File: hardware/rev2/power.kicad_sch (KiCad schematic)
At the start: 0 parts

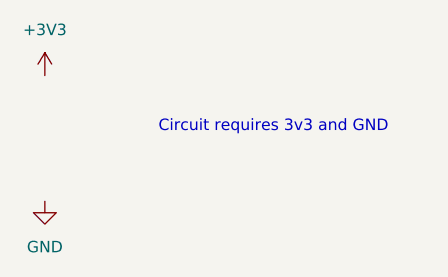
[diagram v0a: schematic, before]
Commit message: fixed some ERC errors and warnings, added USB, assigned a bunch of footprints
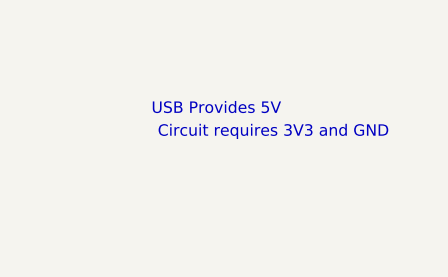
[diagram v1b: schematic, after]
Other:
- note added: "Circuit requires 3V3 and GND"
- note added: "USB Provides 5V"
- note removed: "Circuit requires 3v3 and GND"
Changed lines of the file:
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@@
 	(generator_version "10.0")
 	(paper "A4")
-	(text "Circuit requires 3v3 and GND"
+	(text "USB Provides 5V"
 		(exclude_from_sim no)
-		(at 125.73 80.645 0)
+		(at 119.38 78.74 0)
 		(effects
 			(font
@@
 		)
 	)
-	(symbol
-		(lib_id "power:+3V3")
-		(at 100.33 74.93 0)
-		(unit 1)
-		(body_style 1)
+	(text "Circuit requires 3V3 and GND"
 		(exclude_from_sim no)
-		(in_bom yes)
-		(on_board yes)
-		(in_pos_files yes)
-		(dnp no)
-		(fields_autoplaced yes)
-		(property "Reference" "#PWR059"
-			(at 100.33 78.74 0)
-			(hide yes)
-			(show_name no)
-			(do_not_autoplace no)
-			(effects
-				(font
-					(size 1.27 1.27)
-				)
+		(at 125.73 81.28 0)
+		(effects
+			(font
+				(size 1.27 1.27)
 			)
 		)
-		(property "Value" "+3V3"
-			(at 100.33 69.85 0)
-			(show_name no)
-			(do_not_autoplace no)
-			(effects
-				(font
-					(size 1.27 1.27)
-				)
-			)
-		)
-		(property "Footprint" ""
-			(at 100.33 74.93 0)
-			(hide yes)
-			(show_name no)
-			(do_not_autoplace no)
-			(effects
-				(font
-					(size 1.27 1.27)
-				)
-			)
-		)
-		(property "Datasheet" ""
-			(at 100.33 74.93 0)
-			(hide yes)
-			(show_name no)
-			(do_not_autoplace no)
-			(effects
-				(font
-					(size 1.27 1.27)
-				)
-			)
-		)
-		(property "Description" "Power symbol creates a global label with name \"+3V3\""
-			(at 100.33 74.93 0)
-			(hide yes)
-			(show_name no)
-			(do_not_autoplace no)
-			(effects
-				(font
-					(size 1.27 1.27)
-				)
-			)
-		)
-		(pin "1"
-		)
-		(instances
-			(project "rev2"
-				(path "/9067f306-e23c-4d77-8182-4fa2c4b88902/46484475-7656-401a-9d45-159f5e421427"
-					(reference "#PWR059")
-					(unit 1)
-				)
-			)
-		)
-	)
-	(symbol
-		(lib_id "power:GND")
-		(at 100.33 88.9 0)
-		(unit 1)
-		(body_style 1)
-		(exclude_from_sim no)
-		(in_bom yes)
-		(on_board yes)
-		(in_pos_files yes)
-		(dnp no)
-		(fields_autoplaced yes)
-		(property "Reference" "#PWR060"
-			(at 100.33 95.25 0)
-			(hide yes)
-			(show_name no)
-			(do_not_autoplace no)
-			(effects
-				(font
-					(size 1.27 1.27)
-				)
-			)
-		)
-		(property "Value" "GND"
-			(at 100.33 93.98 0)
-			(show_name no)
-			(do_not_autoplace no)
-			(effects
-				(font
-					(size 1.27 1.27)
-				)
-			)
-		)
-		(property "Footprint" ""
-			(at 100.33 88.9 0)
-			(hide yes)
-			(show_name no)
-			(do_not_autoplace no)
-			(effects
-				(font
-					(size 1.27 1.27)
-				)
-			)
-		)
-		(property "Datasheet" ""
-			(at 100.33 88.9 0)
-			(hide yes)
-			(show_name no)
-			(do_not_autoplace no)
-			(effects
-				(font
-					(size 1.27 1.27)
-				)
-			)
-		)
-		(property "Description" "Power symbol creates a global label with name \"GND\" , ground"
-			(at 100.33 88.9 0)
-			(hide yes)
-			(show_name no)
-			(do_not_autoplace no)
-			(effects
-				(font
-					(size 1.27 1.27)
-				)
-			)
-		)
-		(pin "1"
-		)
-		(instances
-			(project "rev2"
-				(path "/9067f306-e23c-4d77-8182-4fa2c4b88902/46484475-7656-401a-9d45-159f5e421427"
-					(reference "#PWR060")
-					(unit 1)
-				)
-			)
-		)

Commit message: ESP32 approaching final schematic. tidied up a lot and changed GPIO pins.
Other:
- company: (none) -> MMCX11
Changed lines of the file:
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@@
 	(generator_version "10.0")
 	(paper "A4")
+	(title_block
+		(company "MMCX11")
+	)
 	(text "USB Provides 5V"
 		(exclude_from_sim no)

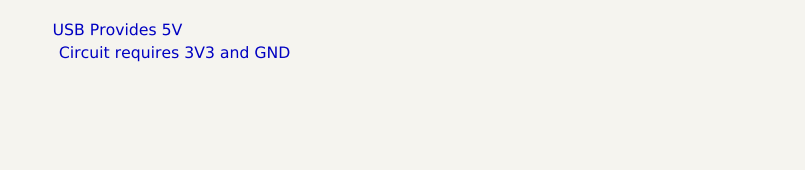
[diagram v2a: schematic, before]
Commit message: set all applicable components for sx1262
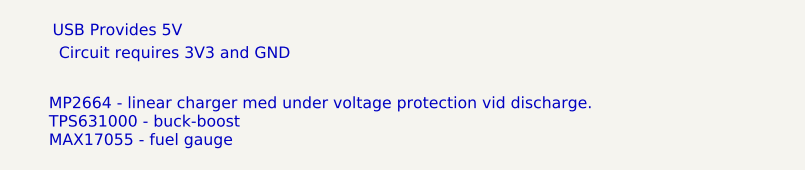
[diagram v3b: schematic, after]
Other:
- note added: "MP2664 - linear charger med under voltage protection vid discharge. TPS631000 - buck-boost MAX17055 - fuel gauge"
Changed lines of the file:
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@@
 		(company "MMCX11")
+	)
+	(text "MP2664 - linear charger med under voltage protection vid discharge.\nTPS631000 - buck-boost\nMAX17055 - fuel gauge"
+		(exclude_from_sim no)
+		(at 111.76 88.9 0)
+		(effects
+			(font
+				(size 1.27 1.27)
+			)
+			(justify left)
+		)
 	)
 	(text "USB Provides 5V"

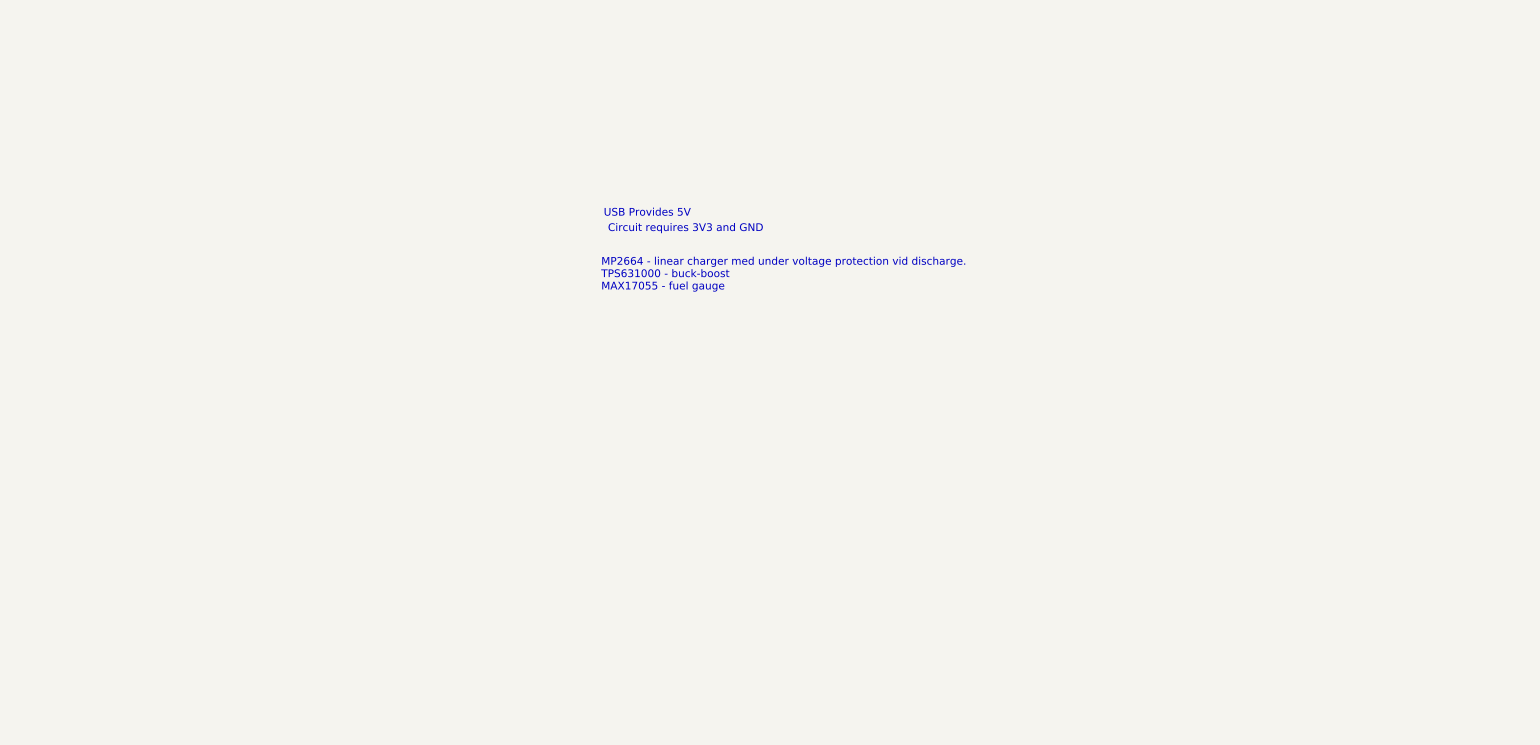
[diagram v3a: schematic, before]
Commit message: Started work on power.kicad_sch
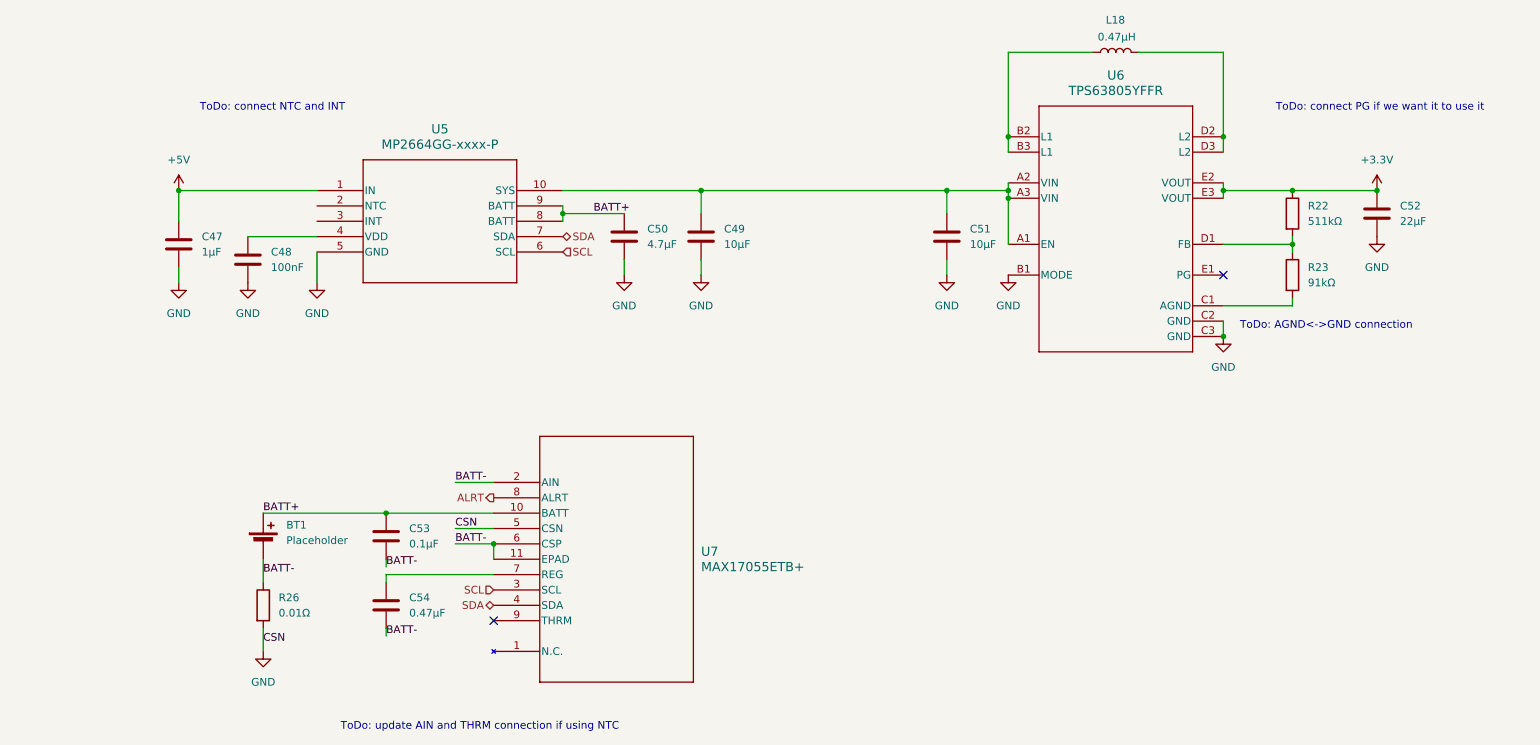
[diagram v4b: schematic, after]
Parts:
- added BT1: Placeholder, symbol Device:Battery_Cell
- added C47: 1µF, symbol Device:C
- added C48: 100nF, symbol Device:C
- added C49, C51: 10µF, symbol Device:C
- added C50: 4.7µF, symbol Device:C
- added C52: 22µF, symbol Device:C
- added C53: 0.1µF, symbol Device:C
- added C54: 0.47µF, symbol Device:C
- added L18: 0.47µH, symbol Device:L
- added R22: 511kΩ, symbol Device:R
- added R23: 91kΩ, symbol Device:R
- added R26: 0.01Ω, symbol Device:R
- added U5: MP2664GG-xxxx-P, QFN-2x2_MP2664_MNP, symbol _symbols:MP2664GG-xxxx-P
- added U6: TPS63805YFFR, YFF0015AHAN, symbol _symbols:TPS63805YFFR
- added U7: MAX17055ETB+, 21-100013A_T102A2+1C_MXM, symbol _symbols:MAX17055ETB+
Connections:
- new net: C49.1, C51.1, U5.10 (SYS), U6.A1 (EN), U6.A2 (VIN), U6.A3 (VIN)
- new net: C48.1, U5.4 (VDD)
- new net: C54.1, U7.7 (REG)
- new net: R22.2, R23.1, U6.D1 (FB)
- new net: L18.1, U6.B2 (L1), U6.B3 (L1)
- new net: R23.2, U6.C1 (AGND)
- new net: L18.2, U6.D2 (L2), U6.D3 (L2)
- new net +3.3V: C52.1, R22.1, U6.E2 (VOUT), U6.E3 (VOUT)
- new net +5V: C47.1, U5.1 (IN)
- new net ALRT: U7.8 (ALRT)
- new net BATT+: BT1.1 (+), C50.1, C53.1, U5.8 (BATT), U5.9 (BATT), U7.10 (BATT)
- new net BATT-: BT1.2 (-), C53.2, C54.2, R26.1, U7.11 (EPAD), U7.2 (AIN), U7.6 (CSP)
- new net GND: C47.2, C48.2, C49.2, C50.2, C51.2, C52.2, R26.2, U5.5 (GND), U6.B1 (MODE), U6.C2 (GND), U6.C3 (GND), U7.5 (CSN)
- new net SCL: U5.6 (SCL), U7.3 (SCL)
- new net SDA: U5.7 (SDA), U7.4 (SDA)
- no-connect marks 0 -> 2
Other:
- note added: "ToDo: AGND<->GND connection"
- note added: "ToDo: connect NTC and INT"
- note added: "ToDo: connect PG if we want it to use it"
- note added: "ToDo: update AIN and THRM connection if using NTC"
- note removed: "Circuit requires 3V3 and GND"
- note removed: "MP2664 - linear charger med under voltage protection vid discharge. TPS631000 - buck-boost MAX17055 - fuel gauge"
- note removed: "USB Provides 5V"

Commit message: Small modifications to power schematic
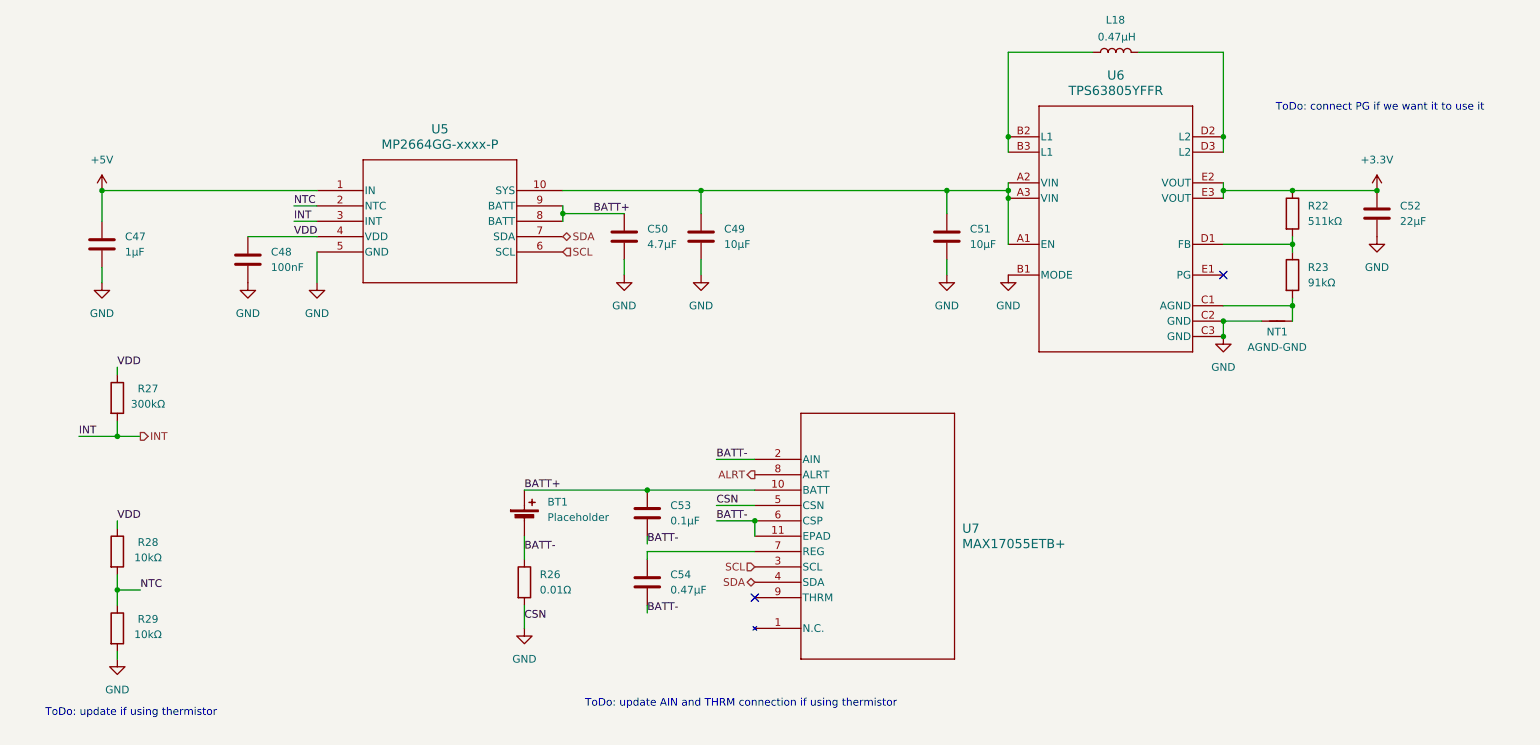
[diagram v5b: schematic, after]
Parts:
- added NT1: AGND-GND, symbol Device:NetTie_2
- added R27: 300kΩ, symbol Device:R
- added R28, R29: 10kΩ, symbol Device:R
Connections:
- net GND: now also NT1.1, R29.2
- net NTC: now reaches U5.2 (NTC)
- net NTC: now also R28.2, R29.1
- net INT: now reaches U5.3 (INT)
- net INT: now also R27.2
- net VDD: now reaches C48.1, U5.4 (VDD)
- net VDD: now also R27.1, R28.1
- net at R23.2, U6.C1 (AGND): now also NT1.2
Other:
- note added: "ToDo: update AIN and THRM connection if using thermistor"
- note added: "ToDo: update if using thermistor"
- note removed: "ToDo: AGND<->GND connection"
- note removed: "ToDo: connect NTC and INT"
- note removed: "ToDo: update AIN and THRM connection if using NTC"
- moved on the sheet: BT1, C47, C53, C54, R26, U7

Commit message: modified layout
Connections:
- net +3.3V renamed +3V3
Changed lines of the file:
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@@
 			)
 		)
-		(property "Value" "+3.3V"
-			(at 240.03 69.85 0)
+		(property "Value" "+3V3"
+			(at 242.57 73.6599 0)
 			(show_name no)
 			(do_not_autoplace no)
@@
 					(size 1.27 1.27)
 				)
+				(justify left)
 			)
 		)
